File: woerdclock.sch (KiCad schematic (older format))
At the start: 88 parts, among them K1 Sound, K10 WS2812B_OUT, K11 WS2812B_IN, K12 WS2812B_IN, K13 WS2812B_OUT, K14 WS2812B_OUT, K15 WS2812B_IN, K16 WS2812B_IN, K17 WS2812B_OUT, K18 WS2812B_OUT, K19 WS2812B_IN, K2 IR, K20 WS2812B_IN, K21 WS2812B_OUT, K22 WS2812B_OUT, K23 WS2812B_IN, K24 WS2812B_IN, K25 WS2812B_OUT, K26 WS2812B_OUT, K27 WS2812B_IN, K3 3V3, K4 WS2812B_OUT, K5 WS2812B_OUT, K6 WS2812B_IN, K7 WS2812B_IN, K8 WS2812B_IN, K9 WS2812B_OUT, P10 CONN_1, P11 CONN_3X2, P12 CONN_1, P13 CONN_1, P14 CONN_1, P15 CONN_1, P16 CONN_1, P17 CONN_1, P4 CONN_1, P5 CONN_1, P6 CONN_1, P7 CONN_1, P8 CONN_3X2, P9 CONN_1, SW1 up, SW2 ok, SW3 down, U1 RFM12B, U10 DCF77, U11 DHT, U14 SD-CARD, U2 RTC_MODUL, U3 ARDUINO_PRO_MICRO, U4 BH1750FVI_MODULE, U5 5V 8A -Co+, U8 ESP8266, U9 10DOF

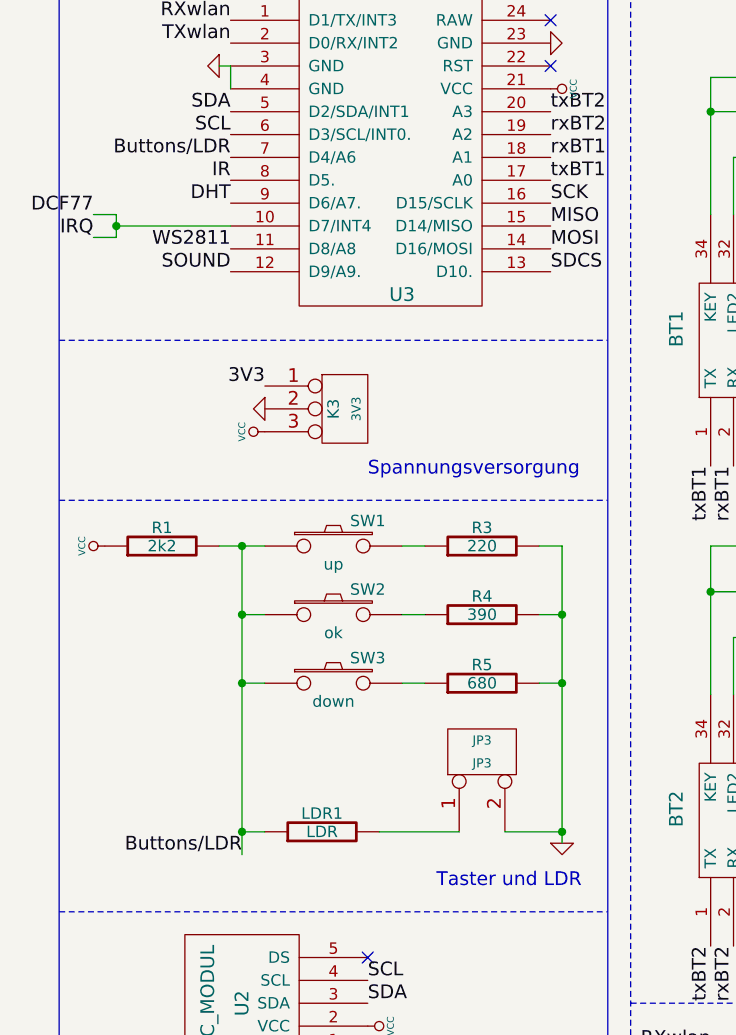
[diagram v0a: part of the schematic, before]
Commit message: DCF77, RFM12B selection via jumper.
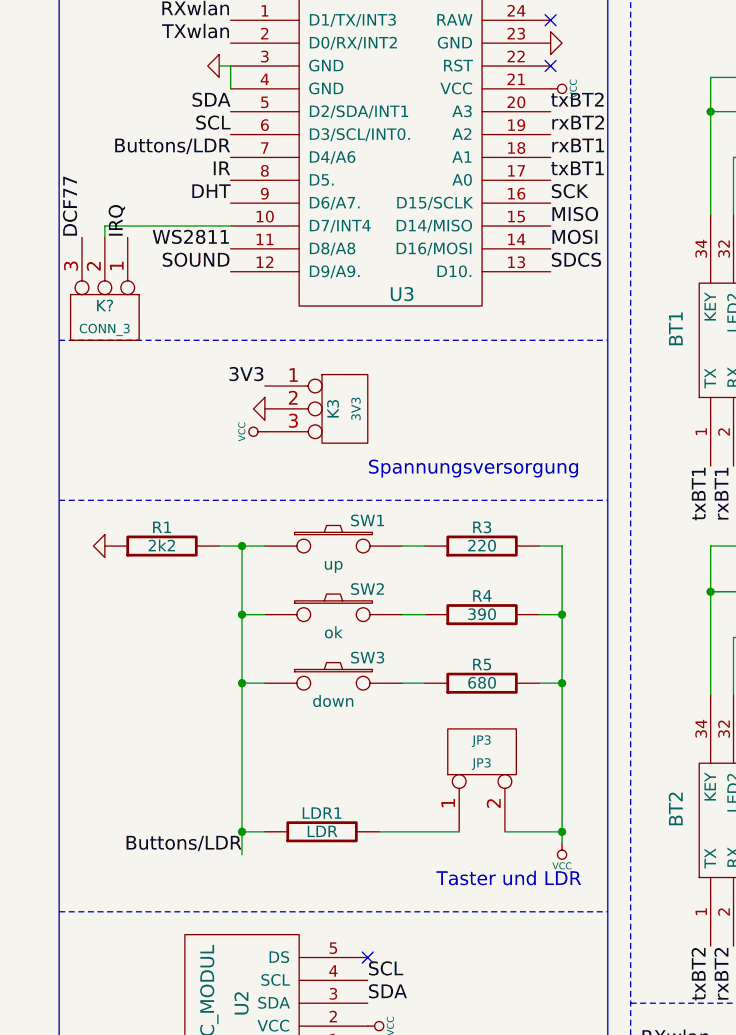
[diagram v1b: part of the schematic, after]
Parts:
- added K?: CONN_3, symbol CONN_3
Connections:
- net DCF77: now also K?.3 (P3); no longer U1.2 (nIRQ), U3.10 (D7/INT4)
- net GND: now also R1.1; no longer JP3.2 (PM), R3.2, R4.2, R5.2
- net VCC: now also JP3.2 (PM), R3.2, R4.2, R5.2; no longer R1.1
- new net: K?.2 (PM), U3.10 (D7/INT4)
- new net IRQ: K?.1 (P1), U1.2 (nIRQ)
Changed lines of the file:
@@
 Text Label 1350 1450 2    60   ~ 0
 Buttons/LDR
-Text Label 750  1700 2    60   ~ 0
+Text Label 700  1800 1    60   ~ 0
 DCF77
 Text Label 6600 3050 3    60   ~ 0
@@
 L GND #PWR010
 U 1 1 5446A9FD
+P 800 3150
+F 0 "#PWR010" H 800 3150 30  0001 C CNN
+F 1 "GND" H 800 3080 30  0001 C CNN
+F 2 "" H 800 3150 60  0001 C CNN
+F 3 "" H 800 3150 60  0001 C CNN
+	1    800  3150
+	0    1    1    0
+$EndComp
+Text Label 1400 4500 2    60   ~ 0
+Buttons/LDR
+$Comp
+L VCC #PWR011
+U 1 1 5446A989
 P 2800 4450
-F 0 "#PWR010" H 2800 4450 30  0001 C CNN
-F 1 "GND" H 2800 4380 30  0001 C CNN
+F 0 "#PWR011" H 2800 4550 30  0001 C CNN
+F 1 "VCC" H 2800 4550 30  0000 C CNN
 F 2 "" H 2800 4450 60  0001 C CNN
 F 3 "" H 2800 4450 60  0001 C CNN
 	1    2800 4450
-	1    0    0    -1
-$EndComp
-Text Label 1400 4500 2    60   ~ 0
-Buttons/LDR
-$Comp
-L VCC #PWR011
-U 1 1 5446A989
-P 800 3150
-F 0 "#PWR011" H 800 3250 30  0001 C CNN
-F 1 "VCC" H 800 3250 30  0000 C CNN
-F 2 "" H 800 3150 60  0001 C CNN
-F 3 "" H 800 3150 60  0001 C CNN
-	1    800  3150
-	0    -1   -1   0
+	-1   0    0    1
 $EndComp
 $Comp
@@
 Text Label 3250 6650 2    60   ~ 0
 IRQ
-Text Label 750  1800 2    60   ~ 0
+Text Label 900  1800 1    60   ~ 0
 IRQ
-Wire Wire Line
-	1350 1750 850  1750
-Wire Wire Line
-	850  1700 850  1800
-Wire Wire Line
-	850  1700 750  1700
-Wire Wire Line
-	850  1800 750  1800
-Connection ~ 850  1750
 Wire Notes Line
 	1300 8400 1300 10300
@@
 	2050 5900 2050 6100
 Connection ~ 2050 6100
+$Comp
+L CONN_3 K?
+U 1 1 546E37C5
+P 800 2150
+F 0 "K?" V 750 2150 50  0000 C CNN
+F 1 "CONN_3" V 850 2150 40  0000 C CNN
+F 2 "" H 800 2150 60  0000 C CNN
+F 3 "" H 800 2150 60  0000 C CNN
+	1    800  2150
+	0    1    1    0
+$EndComp
+Wire Wire Line
+	1350 1750 800  1750
+Wire Wire Line
+	800  1750 800  1800
 $EndSCHEMATC

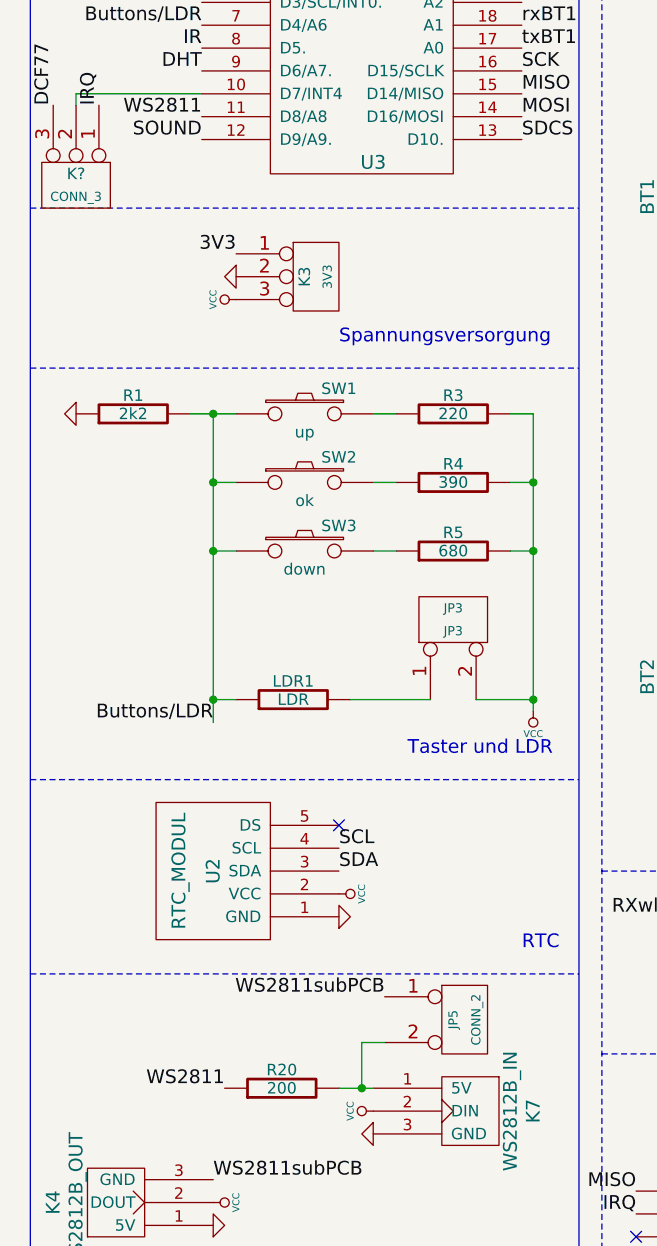
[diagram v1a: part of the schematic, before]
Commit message: Added juper rfm12b / dcf77.
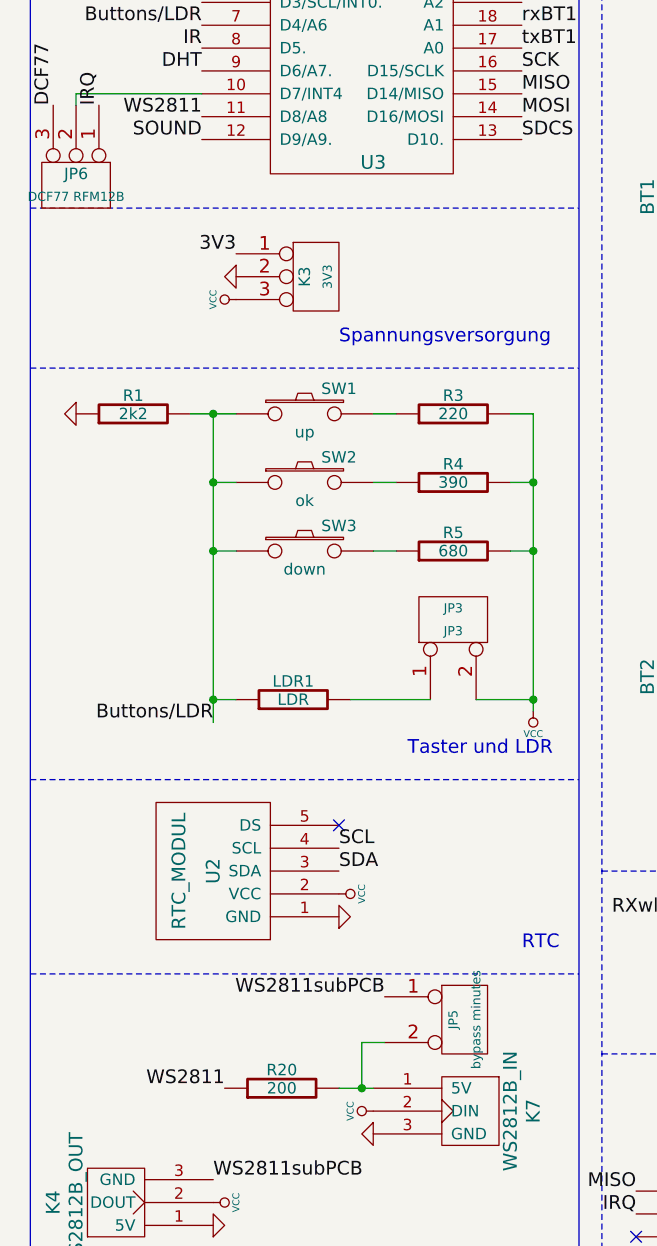
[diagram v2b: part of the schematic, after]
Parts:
- JP5: value CONN_2 -> bypass minutes
- JP6: renamed from K?; value CONN_3 -> DCF77 RFM12B
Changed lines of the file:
@@
 Sheet 1 1
 Title "Wördclock"
-Date "20 nov 2014"
+Date "21 nov 2014"
 Rev "0.2"
 Comp "http://sebastian.setz.name"
@@
 P 2500 5800
 F 0 "JP5" V 2450 5800 40  0000 C CNN
-F 1 "CONN_2" V 2550 5800 40  0000 C CNN
+F 1 "bypass minutes" V 2550 5800 40  0000 C CNN
 F 2 "" H 2500 5800 60  0000 C CNN
 F 3 "" H 2500 5800 60  0000 C CNN
@@
 Connection ~ 2050 6100
 $Comp
-L CONN_3 K?
+L CONN_3 JP6
 U 1 1 546E37C5
 P 800 2150
-F 0 "K?" V 750 2150 50  0000 C CNN
-F 1 "CONN_3" V 850 2150 40  0000 C CNN
+F 0 "JP6" V 750 2150 50  0000 C CNN
+F 1 "DCF77   RFM12B" V 850 2150 40  0000 C CNN
 F 2 "" H 800 2150 60  0000 C CNN
 F 3 "" H 800 2150 60  0000 C CNN

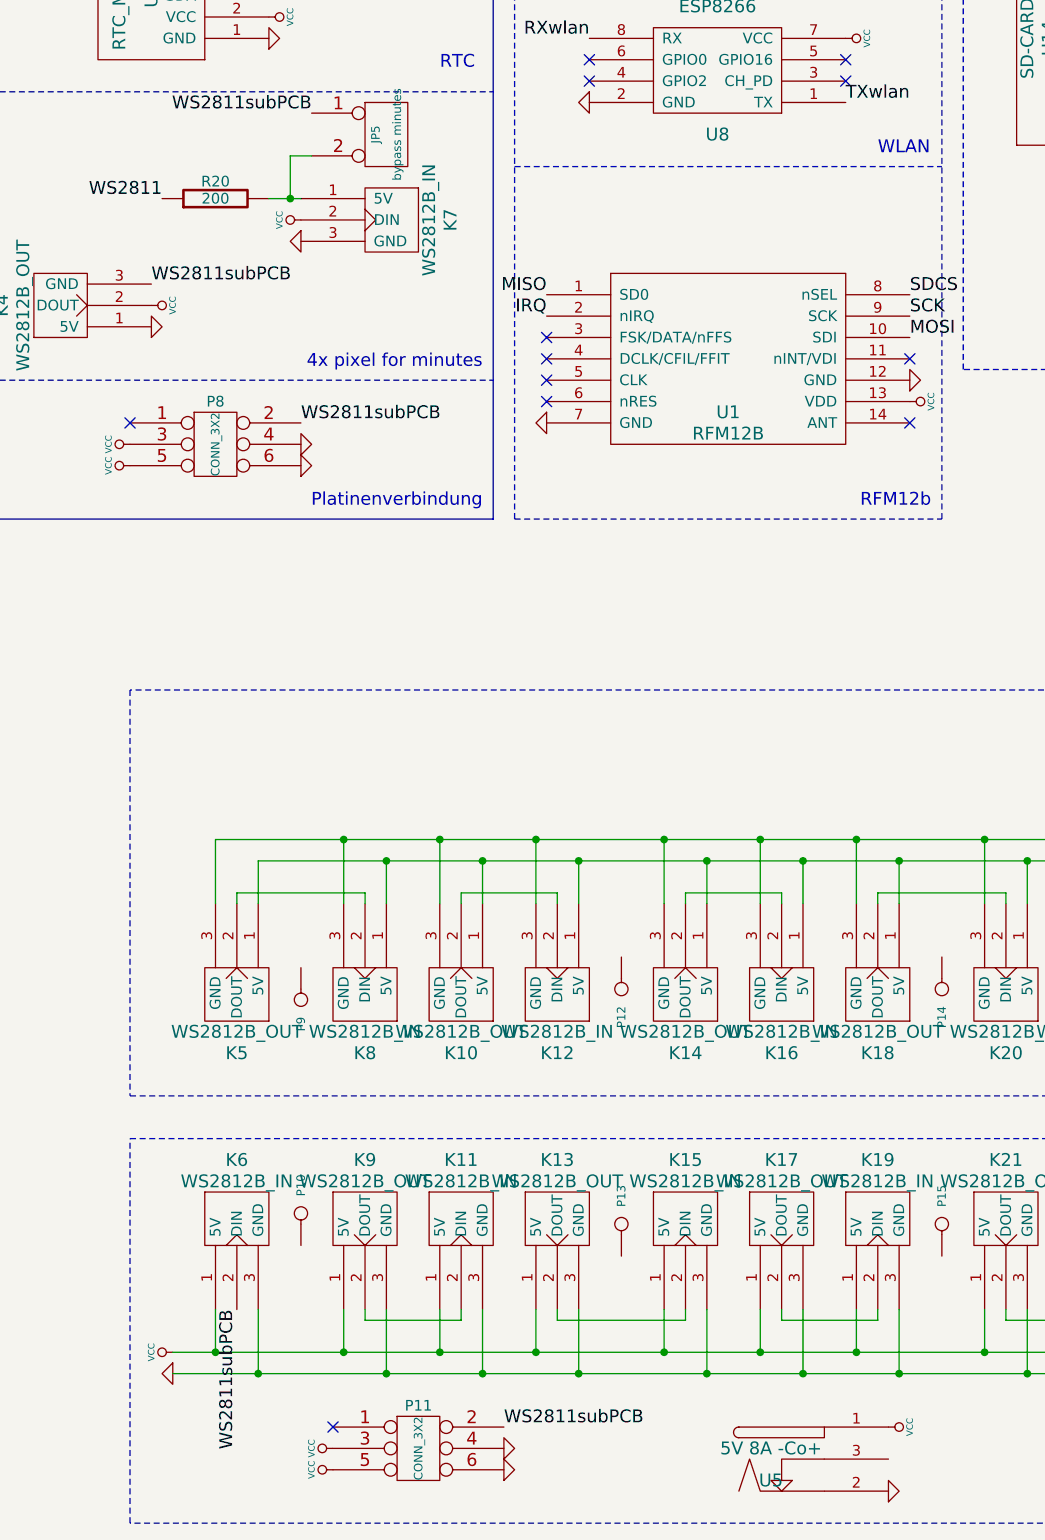
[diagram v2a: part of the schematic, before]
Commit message: reversed gnd <-> 5v for minutes strip.fixed. added slikscreen text for strip soldering pads.
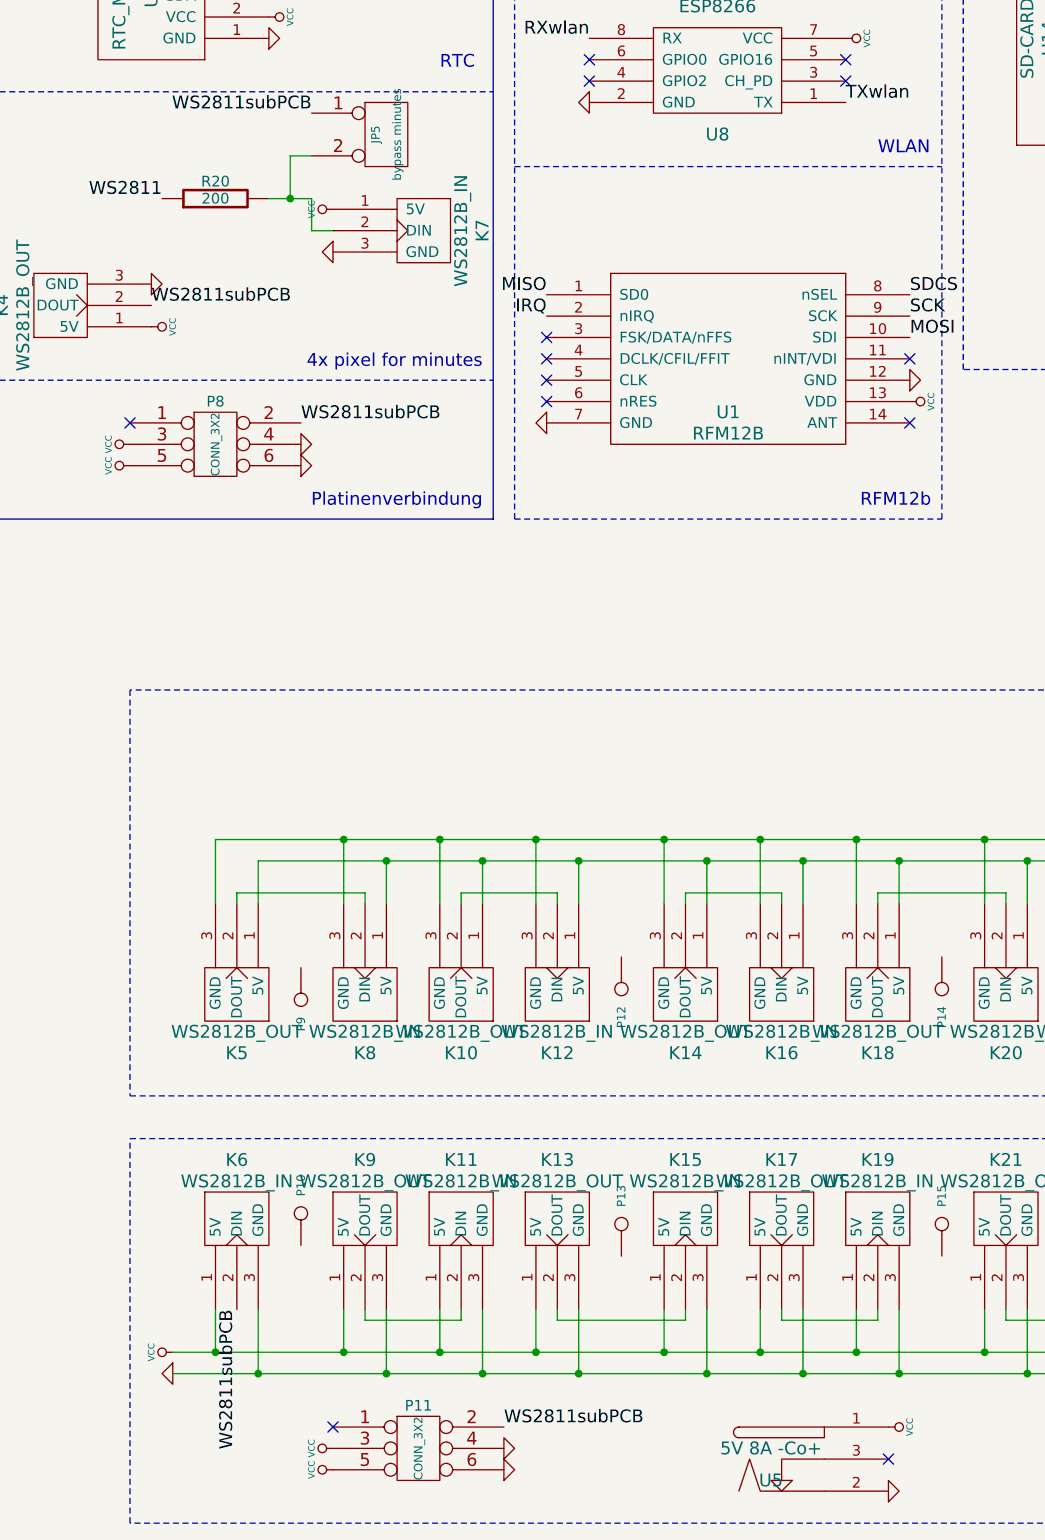
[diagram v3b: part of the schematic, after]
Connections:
- net GND: now also K4.3 (GND); no longer K4.1 (5V)
- net VCC: now also K4.1 (5V), K7.1 (5V); no longer K4.2 (DOUT), K7.2 (DIN)
- net WS2811subPCB: now also K4.2 (DOUT); no longer K4.3 (GND)
- net at JP5.2 (PM), R20.2: now also K7.2 (DIN); no longer K7.1 (5V)
- no-connect marks 21 -> 22
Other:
- moved on the sheet: K7
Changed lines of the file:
@@
 Sheet 1 1
 Title "Wördclock"
-Date "21 nov 2014"
+Date "22 nov 2014"
 Rev "0.2"
 Comp "http://sebastian.setz.name"
@@
 	1    0    0    -1
 $EndComp
-Text Label 1400 6500 0    60   ~ 0
+Text Label 1400 6600 0    60   ~ 0
 WS2811subPCB
 Text Label 2100 7150 0    60   ~ 0
@@
 L GND #PWR038
 U 1 1 546A1681
-P 2100 6300
-F 0 "#PWR038" H 2100 6300 30  0001 C CNN
-F 1 "GND" H 2100 6230 30  0001 C CNN
-F 2 "" H 2100 6300 60  0001 C CNN
-F 3 "" H 2100 6300 60  0001 C CNN
-	1    2100 6300
+P 2250 6350
+F 0 "#PWR038" H 2250 6350 30  0001 C CNN
+F 1 "GND" H 2250 6280 30  0001 C CNN
+F 2 "" H 2250 6350 60  0001 C CNN
+F 3 "" H 2250 6350 60  0001 C CNN
+	1    2250 6350
 	0    1    1    0
 $EndComp
@@
 L VCC #PWR039
 U 1 1 546A1687
-P 2100 6200
-F 0 "#PWR039" H 2100 6300 30  0001 C CNN
-F 1 "VCC" H 2100 6300 30  0000 C CNN
-F 2 "" H 2100 6200 60  0001 C CNN
-F 3 "" H 2100 6200 60  0001 C CNN
-	1    2100 6200
+P 2250 6150
+F 0 "#PWR039" H 2250 6250 30  0001 C CNN
+F 1 "VCC" H 2250 6250 30  0000 C CNN
+F 2 "" H 2250 6150 60  0001 C CNN
+F 3 "" H 2250 6150 60  0001 C CNN
+	1    2250 6150
 	0    -1   -1   0
 $EndComp
@@
 L VCC #PWR040
 U 1 1 546A168D
-P 1400 6600
-F 0 "#PWR040" H 1400 6700 30  0001 C CNN
-F 1 "VCC" H 1400 6700 30  0000 C CNN
-F 2 "" H 1400 6600 60  0001 C CNN
-F 3 "" H 1400 6600 60  0001 C CNN
-	1    1400 6600
-	0    1    1    0
-$EndComp
-$Comp
-L GND #PWR041
-U 1 1 546A1693
 P 1400 6700
-F 0 "#PWR041" H 1400 6700 30  0001 C CNN
-F 1 "GND" H 1400 6630 30  0001 C CNN
+F 0 "#PWR040" H 1400 6800 30  0001 C CNN
+F 1 "VCC" H 1400 6800 30  0000 C CNN
 F 2 "" H 1400 6700 60  0001 C CNN
 F 3 "" H 1400 6700 60  0001 C CNN
 	1    1400 6700
+	0    1    1    0
+$EndComp
+$Comp
+L GND #PWR041
+U 1 1 546A1693
+P 1400 6500
+F 0 "#PWR041" H 1400 6500 30  0001 C CNN
+F 1 "GND" H 1400 6430 30  0001 C CNN
+F 2 "" H 1400 6500 60  0001 C CNN
+F 3 "" H 1400 6500 60  0001 C CNN
+	1    1400 6500
 	0    -1   -1   0
 $EndComp
@@
 L WS2812B_IN K7
 U 1 1 546B01E4
-P 2600 6200
-F 0 "K7" H 2600 6400 60  0000 C CNN
-F 1 "WS2812B_IN" H 2600 6300 60  0000 C CNN
-F 2 "" H 2600 6200 60  0000 C CNN
-F 3 "" H 2600 6200 60  0000 C CNN
-	1    2600 6200
+P 2750 6250
+F 0 "K7" H 2750 6450 60  0000 C CNN
+F 1 "WS2812B_IN" H 2750 6350 60  0000 C CNN
+F 2 "" H 2750 6250 60  0000 C CNN
+F 3 "" H 2750 6250 60  0000 C CNN
+	1    2750 6250
 	0    1    1    0
 $EndComp
@@
 WS2811subPCB
 Wire Wire Line
-	1950 6100 2100 6100
-Wire Wire Line
 	2150 5900 2050 5900
 Wire Wire Line
 	2050 5900 2050 6100
-Connection ~ 2050 6100
 $Comp
 L CONN_3 JP6
@@
 Wire Wire Line
 	800  1750 800  1800
+NoConn ~ 4850 12000
+Wire Wire Line
+	1950 6100 2150 6100
+Wire Wire Line
+	2150 6100 2150 6250
+Wire Wire Line
+	2150 6250 2250 6250
+Connection ~ 2050 6100
 $EndSCHEMATC
